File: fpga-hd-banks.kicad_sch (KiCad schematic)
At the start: 18 parts, among them Q4 BSS138PW, Q5 BSS138PW, Q6 BSS138PW, Q7 BSS138PW, Q8 BSS138PW, U34 XCAU25P-2FFVB676I, Y3 Oscillator_100MHz_ASFL1

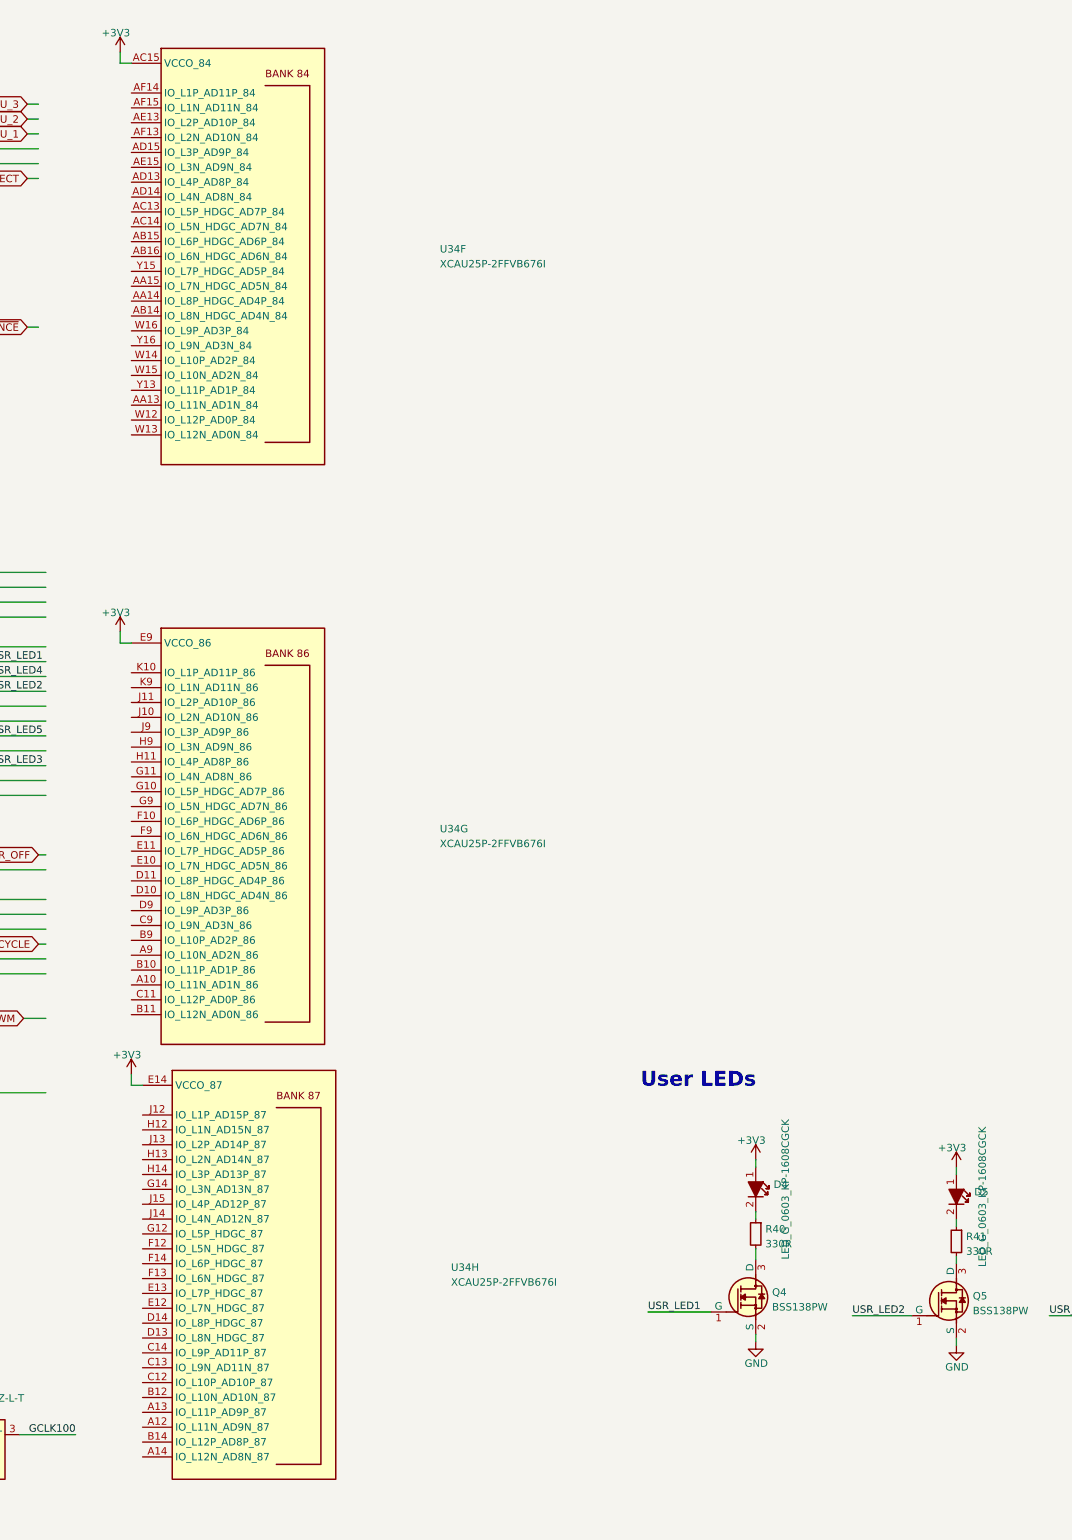
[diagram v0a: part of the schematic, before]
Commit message: [#66312] Continued HDMI schematic connections
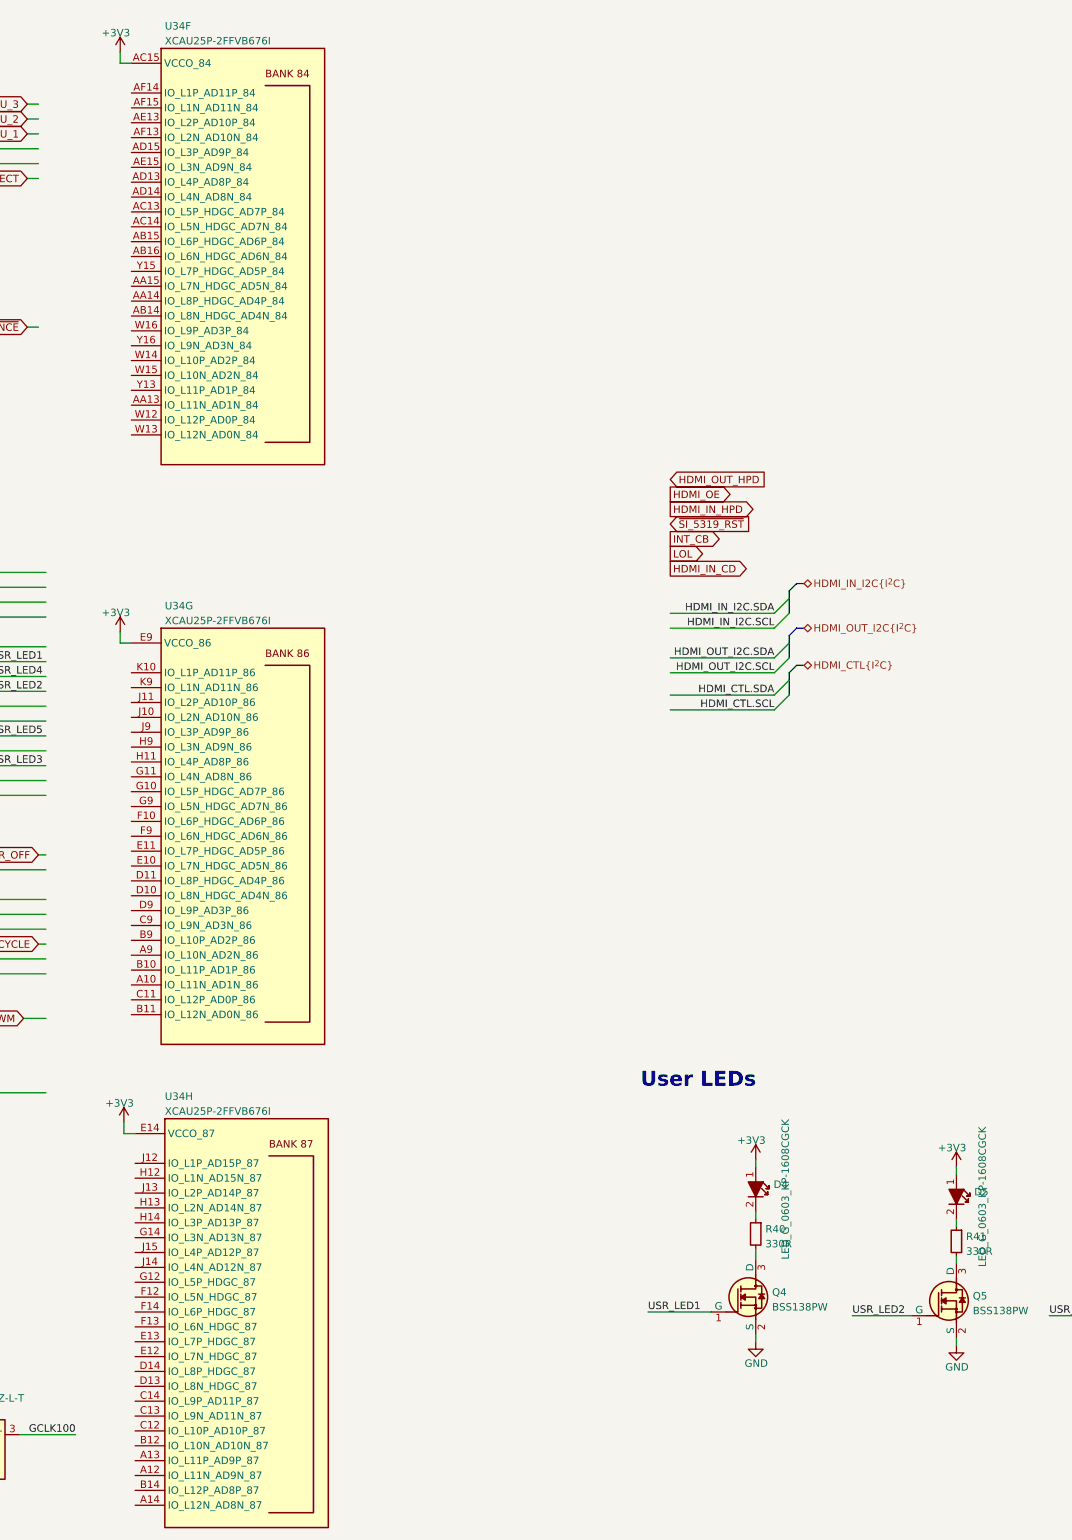
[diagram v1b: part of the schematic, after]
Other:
- moved on the sheet: U34H

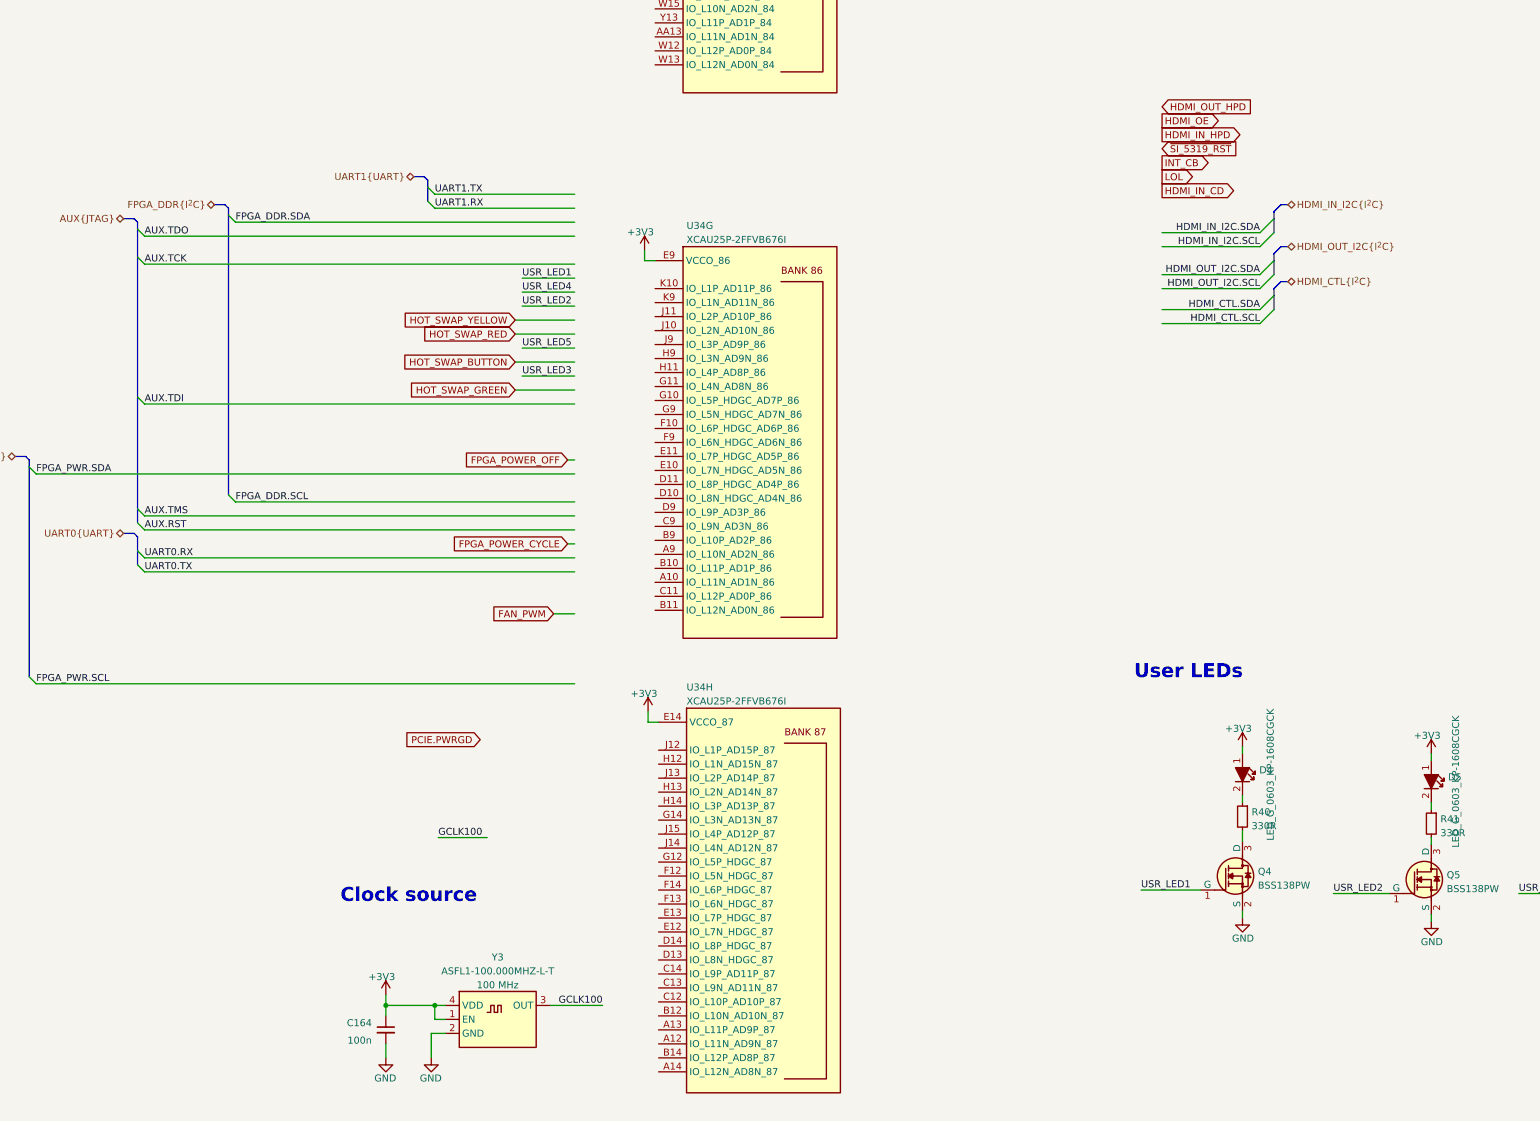
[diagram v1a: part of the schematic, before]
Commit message: [#66312] Connected LS HDMI signals
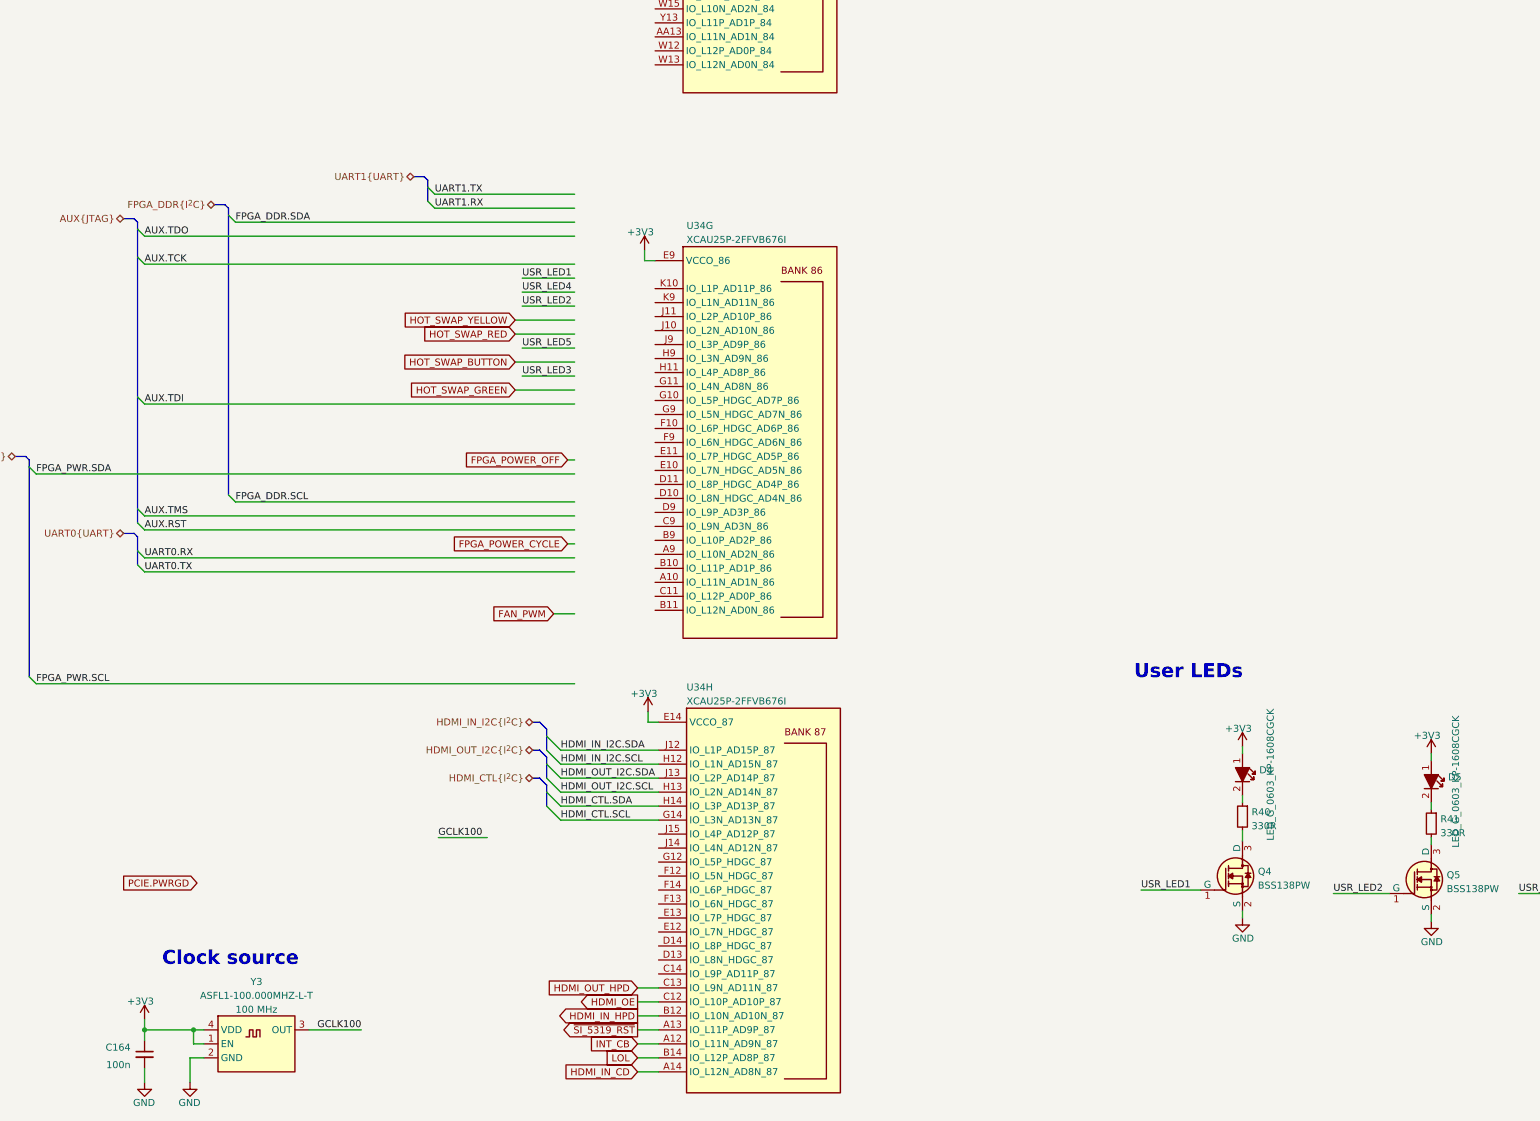
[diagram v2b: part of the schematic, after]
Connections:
- net HDMI_CTL.SCL: now also U34.G14 (IO_L3N_AD13N_87)
- net HDMI_CTL.SDA: now also U34.H14 (IO_L3P_AD13P_87)
- net HDMI_IN_CD: now also U34.A14 (IO_L12N_AD8N_87)
- net HDMI_IN_HPD: now also U34.B12 (IO_L10N_AD10N_87)
- net HDMI_IN_I2C.SCL: now also U34.H12 (IO_L1N_AD15N_87)
- net HDMI_IN_I2C.SDA: now also U34.J12 (IO_L1P_AD15P_87)
- net HDMI_OE: now also U34.C12 (IO_L10P_AD10P_87)
- net HDMI_OUT_HPD: now also U34.C13 (IO_L9N_AD11N_87)
- net HDMI_OUT_I2C.SCL: now also U34.H13 (IO_L2N_AD14N_87)
- net HDMI_OUT_I2C.SDA: now also U34.J13 (IO_L2P_AD14P_87)
- net INT_CB: now also U34.A12 (IO_L11N_AD9N_87)
- net LOL: now also U34.B14 (IO_L12P_AD8P_87)
- net ~{SI_5319_RST}: now also U34.A13 (IO_L11P_AD9P_87)
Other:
- moved on the sheet: C164, Y3

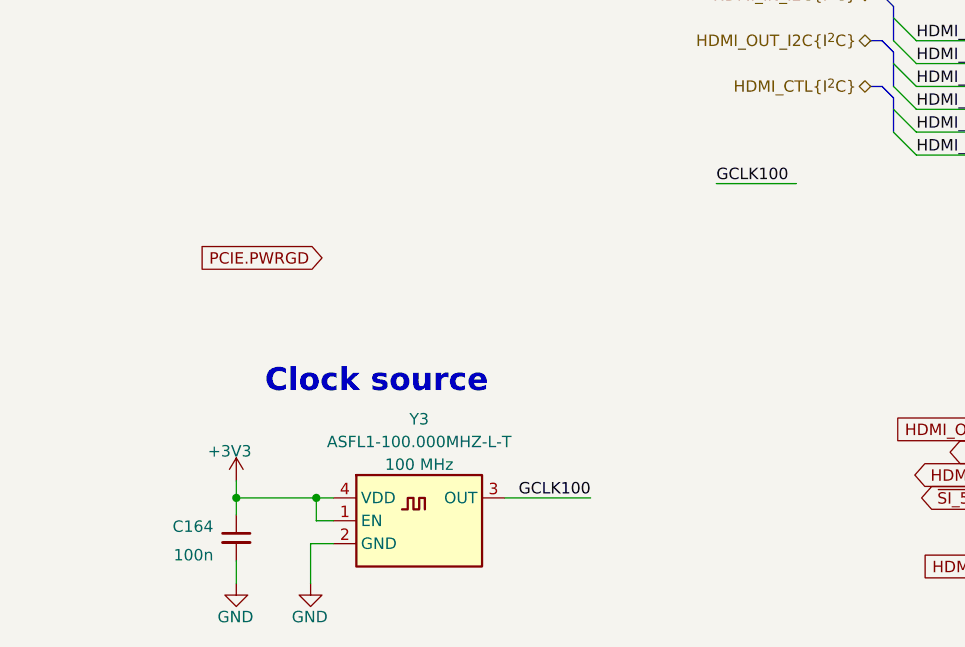
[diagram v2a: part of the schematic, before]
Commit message: [#66312] Added 100MHz LVDS clock source
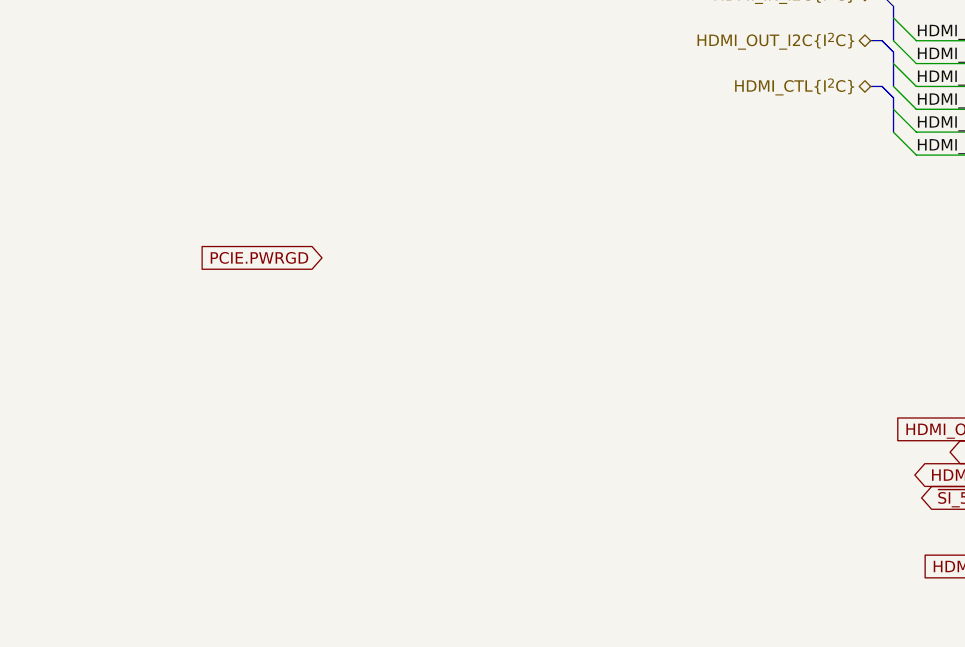
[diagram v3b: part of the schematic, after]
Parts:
- removed C164: C_100n_0402, antmicro-footprints:C_0402_1005Metric, symbol antmicroCapacitors0402:C_100n_0402
- removed Y3: Oscillator_100MHz_ASFL1, antmicro-footprints:Oscillator_SMD_Abracon_ASFL1-4Pin_5.0x3.2mm, symbol antmicroOscillators:Oscillator_100MHz_ASFL1
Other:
- note removed: "Clock source"

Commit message: [#67402] Connect low speed signals and interfaces to the HD banks
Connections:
- net AUX.RST: now also U34.A9 (IO_L10N_AD2N_86)
- net AUX.TCK: now also U34.D9 (IO_L9P_AD3P_86)
- net AUX.TDI: now also U34.C9 (IO_L9N_AD3N_86)
- net AUX.TDO: now also U34.D10 (IO_L8N_HDGC_AD4N_86)
- net AUX.TMS: now also U34.B9 (IO_L10P_AD2P_86)
- net FAN_PWM: now also U34.AA14 (IO_L8P_HDGC_AD4P_84)
- net FPGA_DDR.SCL: now also U34.W15 (IO_L10N_AD2N_84)
- net FPGA_DDR.SDA: now also U34.W14 (IO_L10P_AD2P_84)
- net FPGA_POWER_CYCLE: now also U34.AA15 (IO_L7N_HDGC_AD5N_84)
- net FPGA_POWER_OFF: now also U34.Y15 (IO_L7P_HDGC_AD5P_84)
- net FPGA_PWR.SCL: now also U34.W13 (IO_L12N_AD0N_84)
- net FPGA_PWR.SDA: now also U34.W12 (IO_L12P_AD0P_84)
- net HOT_SWAP_BUTTON: now also U34.AF13 (IO_L2N_AD10N_84)
- net HOT_SWAP_GREEN: now also U34.AE13 (IO_L2P_AD10P_84)
- net HOT_SWAP_RED: now also U34.AF15 (IO_L1N_AD11N_84)
- net HOT_SWAP_YELLOW: now also U34.AF14 (IO_L1P_AD11P_84)
- net PCIE.PWRGD: now also U34.AC14 (IO_L5N_HDGC_AD7N_84)
- net UART0.RX: now also U34.F10 (IO_L6P_HDGC_AD6P_86)
- net UART0.TX: now also U34.F9 (IO_L6N_HDGC_AD6N_86)
- net UART1.RX: now also U34.G9 (IO_L5N_HDGC_AD7N_86)
- net UART1.TX: now also U34.G10 (IO_L5P_HDGC_AD7P_86)
- net USR_LED1: now also U34.K10 (IO_L1P_AD11P_86)
- net USR_LED2: now also U34.K9 (IO_L1N_AD11N_86)
- net USR_LED3: now also U34.J11 (IO_L2P_AD10P_86)
- net USR_LED4: now also U34.J10 (IO_L2N_AD10N_86)
- net USR_LED5: now also U34.J9 (IO_L3P_AD9P_86)
- net ~{DDR_PRESENCE}: now also U34.AD13 (IO_L4P_AD8P_84)
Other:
- note added: "Left FPGA side"
- note added: "One device on the FPGA_PWR bus (TMP451AIDQFR) operates at 1V8 - can be changed to 3V3"
- note added: "Right FPGA side"
- moved on the sheet: D4, D5, D6, D7, D8, Q4, Q5, Q6, Q7, Q8, R40, R41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

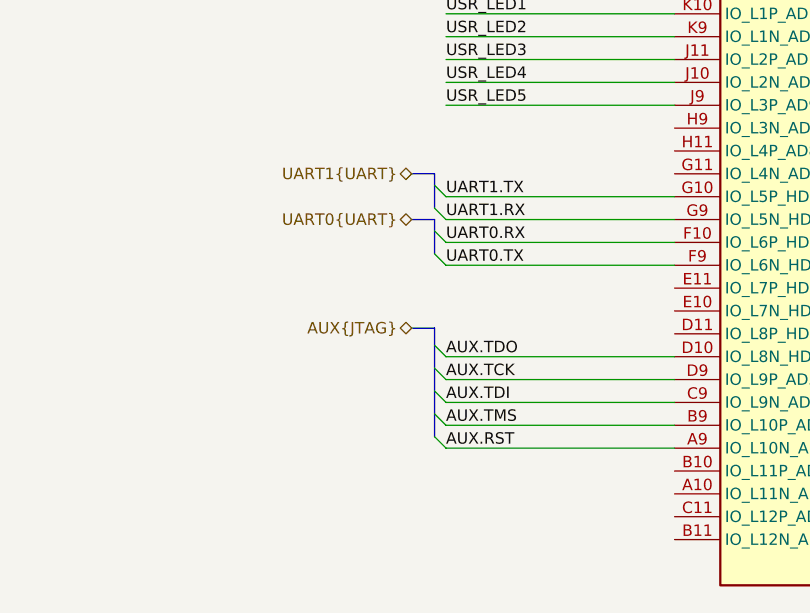
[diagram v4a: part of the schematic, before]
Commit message: [#67402] Optimize connection in bank 86
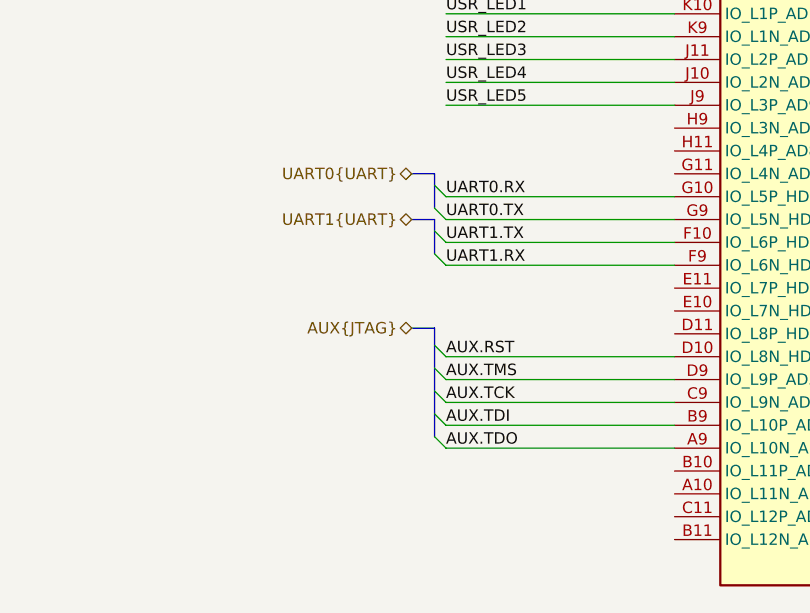
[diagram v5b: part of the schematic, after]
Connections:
- net AUX.RST: now also U34.D10 (IO_L8N_HDGC_AD4N_86); no longer U34.A9 (IO_L10N_AD2N_86)
- net AUX.TCK: now also U34.C9 (IO_L9N_AD3N_86); no longer U34.D9 (IO_L9P_AD3P_86)
- net AUX.TDI: now also U34.B9 (IO_L10P_AD2P_86); no longer U34.C9 (IO_L9N_AD3N_86)
- net AUX.TDO: now also U34.A9 (IO_L10N_AD2N_86); no longer U34.D10 (IO_L8N_HDGC_AD4N_86)
- net AUX.TMS: now also U34.D9 (IO_L9P_AD3P_86); no longer U34.B9 (IO_L10P_AD2P_86)
- net UART0.RX: now also U34.G10 (IO_L5P_HDGC_AD7P_86); no longer U34.F10 (IO_L6P_HDGC_AD6P_86)
- net UART0.TX: now also U34.G9 (IO_L5N_HDGC_AD7N_86); no longer U34.F9 (IO_L6N_HDGC_AD6N_86)
- net UART1.RX: now also U34.F9 (IO_L6N_HDGC_AD6N_86); no longer U34.G9 (IO_L5N_HDGC_AD7N_86)
- net UART1.TX: now also U34.F10 (IO_L6P_HDGC_AD6P_86); no longer U34.G10 (IO_L5P_HDGC_AD7P_86)
